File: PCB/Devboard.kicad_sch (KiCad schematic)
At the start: 0 parts

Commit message: Fix Section 1
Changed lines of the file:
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@@
 	(generator "eeschema")
 	(generator_version "10.0")
-	(paper "E")
-	(sheet
-		(at 292.735 15.24)
+	(paper "A1")
+	(sheet
+		(at 328.93 219.71)
 		(size 43.18 27.305)
 		(exclude_from_sim no)
@@
 		)
 		(property "Sheetname" "DDR4 Memory"
-			(at 292.735 14.5284 0)
+			(at 328.93 218.9984 0)
 			(show_name no)
 			(do_not_autoplace no)
@@
 		)
 		(property "Sheetfile" "schematics/04_Zynq/04b_Zynq_DDR4.kicad_sch"
-			(at 292.735 43.1296 0)
+			(at 328.93 247.5996 0)
 			(show_name no)
 			(do_not_autoplace no)
@@
 	)
 	(sheet
-		(at 158.115 15.24)
+		(at 194.31 219.71)
 		(size 45.085 27.305)
 		(exclude_from_sim no)
@@
 		)
 		(property "Sheetname" "Power Tree"
-			(at 158.115 14.5284 0)
+			(at 194.31 218.9984 0)
 			(show_name no)
 			(do_not_autoplace no)
@@
 		)
 		(property "Sheetfile" "schematics/03_Power_Tree/03_Power_Tree.kicad_sch"
-			(at 158.115 43.1296 0)
+			(at 194.31 247.5996 0)
 			(show_name no)
 			(do_not_autoplace no)
@@
 	)
 	(sheet
-		(at 88.265 15.24)
-		(size 44.45 27.305)
+		(at 118.745 15.24)
+		(size 43.815 27.94)
 		(exclude_from_sim no)
 		(in_bom yes)
@@
 		)
 		(property "Sheetname" "Battery.Charger,Fuel Gauge"
-			(at 88.265 14.5284 0)
+			(at 118.745 14.5284 0)
 			(show_name no)
 			(do_not_autoplace no)
@@
 		)
 		(property "Sheetfile" "schematics/02_Battery/Battery_Charger_FuelGauge.kicad_sch"
-			(at 88.265 43.1296 0)
+			(at 118.745 43.7646 0)
 			(show_name no)
 			(do_not_autoplace no)
@@
 	)
 	(sheet
-		(at 227.33 15.24)
+		(at 263.525 219.71)
 		(size 45.72 27.305)
 		(exclude_from_sim no)
@@
 		)
 		(property "Sheetname" "ZYNQ CORE"
-			(at 227.33 14.5284 0)
+			(at 263.525 218.9984 0)
 			(show_name no)
 			(do_not_autoplace no)
@@
 		)
 		(property "Sheetfile" "schematics/04_Zynq/04a_Zynq_Core.kicad_sch"
-			(at 227.33 43.1296 0)
+			(at 263.525 247.5996 0)
 			(show_name no)
 			(do_not_autoplace no)
@@
 	(sheet
 		(at 15.24 15.24)
-		(size 44.45 27.305)
+		(size 86.36 78.105)
 		(exclude_from_sim no)
 		(in_bom yes)
@@
 		)
 		(property "Sheetname" "Power,Input,Protection"
-			(at 15.24 14.5284 0)
+			(at 43.942 59.182 0)
 			(show_name no)
 			(do_not_autoplace no)
@@
 		)
 		(property "Sheetfile" "schematics/01_Power/Power_Input_Protection.kicad_sch"
-			(at 15.24 43.942 0)
-			(show_name no)
-			(do_not_autoplace no)
+			(at 27.178 60.198 0)
+			(show_name no)
+			(do_not_autoplace no)

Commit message: Zynq Added
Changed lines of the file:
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@@
 	)
 	(sheet
-		(at 194.31 219.71)
+		(at 243.205 45.72)
 		(size 45.085 27.305)
 		(exclude_from_sim no)
@@
 		)
 		(property "Sheetname" "Power Tree"
-			(at 194.31 218.9984 0)
+			(at 243.205 45.0084 0)
 			(show_name no)
 			(do_not_autoplace no)
@@
 		)
 		(property "Sheetfile" "schematics/03_Power_Tree/03_Power_Tree.kicad_sch"
-			(at 194.31 247.5996 0)
+			(at 243.205 73.6096 0)
 			(show_name no)
 			(do_not_autoplace no)
@@
 	(sheet
 		(at 118.745 15.24)
-		(size 43.815 27.94)
+		(size 88.9 78.105)
 		(exclude_from_sim no)
 		(in_bom yes)
 		(on_board yes)
 		(dnp no)
-		(fields_autoplaced yes)
 		(stroke
 			(width 0.1524)
@@
 		)
 		(property "Sheetname" "Battery.Charger,Fuel Gauge"
-			(at 118.745 14.5284 0)
+			(at 149.86 59.182 0)
 			(show_name no)
 			(do_not_autoplace no)
@@
 		)
 		(property "Sheetfile" "schematics/02_Battery/Battery_Charger_FuelGauge.kicad_sch"
-			(at 118.745 43.7646 0)
+			(at 132.334 93.98 0)
 			(show_name no)
 			(do_not_autoplace no)
@@
 		)
 		(property "Sheetfile" "schematics/01_Power/Power_Input_Protection.kicad_sch"
-			(at 27.178 60.198 0)
+			(at 29.464 94.234 0)
 			(show_name no)
 			(do_not_autoplace no)

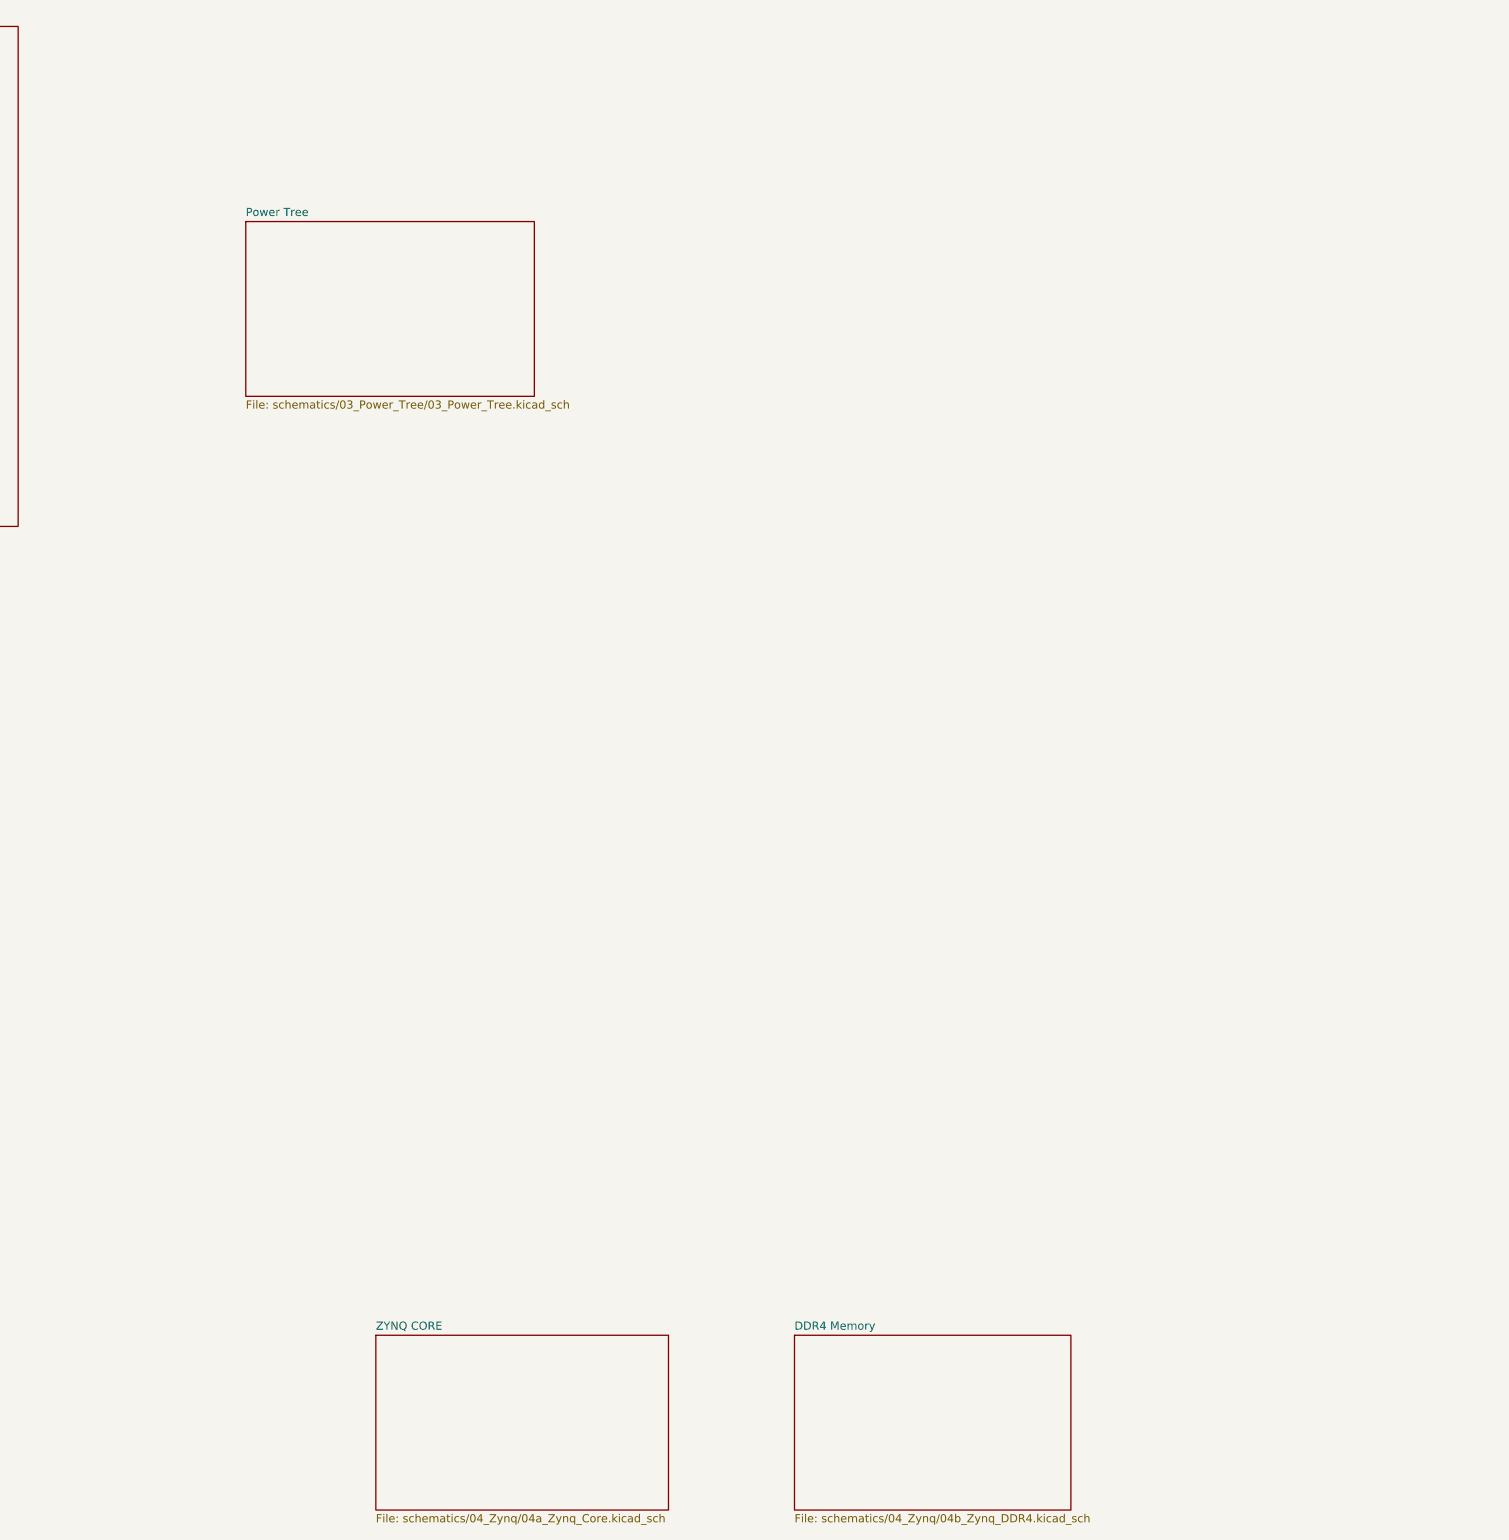
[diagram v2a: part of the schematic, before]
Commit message: Feat: Added zynq decoupling caps
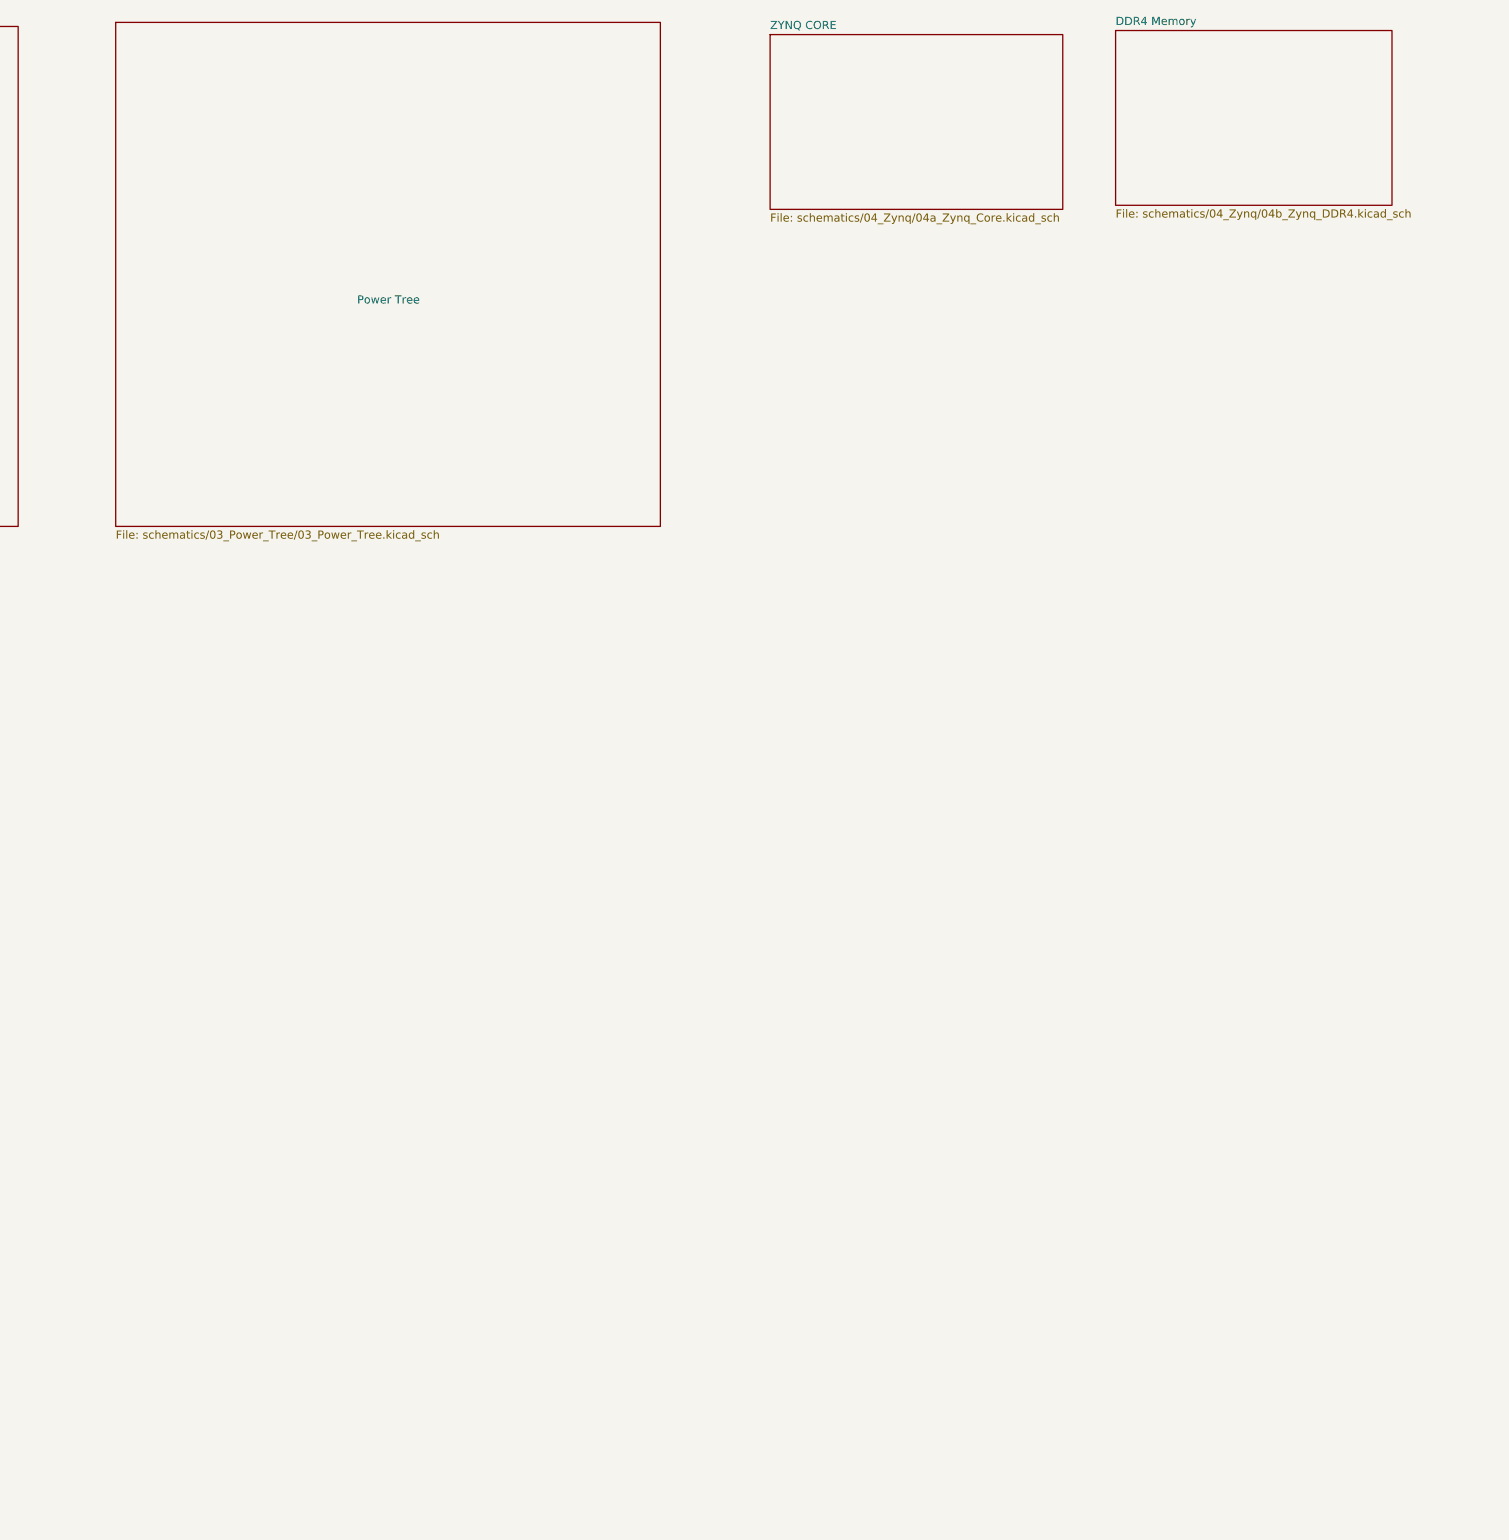
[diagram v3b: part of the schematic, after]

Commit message: Feat: Completed Zynq Core
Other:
- removed sheet DDR4 Memory
- removed sheet ZYNQ CORE
- added sheet Zynq Section (schematics\04_Zynq\04_Zynq.kicad_sch)
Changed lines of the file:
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@@
 	(paper "A2")
-	(sheet
-		(at 379.095 15.875)
-		(size 43.18 27.305)
-		(exclude_from_sim no)
-		(in_bom yes)
-		(on_board yes)
-		(dnp no)
-		(fields_autoplaced yes)
-		(stroke
-			(width 0.1524)
-			(type solid)
-		)
-		(fill
-			(color 0 0 0 0)
-		)
-		(property "Sheetname" "DDR4 Memory"
-			(at 379.095 15.1634 0)
-			(show_name no)
-			(do_not_autoplace no)
-			(effects
-				(font
-					(size 1.27 1.27)
-				)
-				(justify left bottom)
-			)
-		)
-		(property "Sheetfile" "schematics/04_Zynq/04b_Zynq_DDR4.kicad_sch"
-			(at 379.095 43.7646 0)
-			(show_name no)
-			(do_not_autoplace no)
-			(effects
-				(font
-					(size 1.27 1.27)
-				)
-				(justify left top)
-			)
-		)
-		(instances
-			(project "Devboard"
-				(path "/f4f7837f-dd80-4f77-b150-4534de1c10d6"
-					(page "6")
-				)
-			)
-		)
-	)
 	(sheet
 		(at 222.885 14.605)
@@
 	)
 	(sheet
-		(at 325.12 16.51)
-		(size 45.72 27.305)
-		(exclude_from_sim no)
-		(in_bom yes)
-		(on_board yes)
-		(dnp no)
-		(fields_autoplaced yes)
-		(stroke
-			(width 0.1524)
-			(type solid)
-		)
-		(fill
-			(color 0 0 0 0)
-		)
-		(property "Sheetname" "ZYNQ CORE"
-			(at 325.12 15.7984 0)
-			(show_name no)
-			(do_not_autoplace no)
-			(effects
-				(font
-					(size 1.27 1.27)
-				)
-				(justify left bottom)
-			)
-		)
-		(property "Sheetfile" "schematics/04_Zynq/04a_Zynq_Core.kicad_sch"
-			(at 325.12 44.3996 0)
-			(show_name no)
-			(do_not_autoplace no)
-			(effects
-				(font
-					(size 1.27 1.27)
-				)
-				(justify left top)
-			)
-		)
-		(instances
-			(project "Devboard"
-				(path "/f4f7837f-dd80-4f77-b150-4534de1c10d6"
-					(page "5")
-				)
-			)
-		)
-	)
-	(sheet
 		(at 15.24 15.24)
 		(size 86.36 78.105)
@@
 				)
 			)
+		)
+	)
+	(sheet
+		(at 323.215 14.605)
+		(size 82.55 78.74)
+		(exclude_from_sim no)
+		(in_bom yes)
+		(on_board yes)
+		(dnp no)
+		(fields_autoplaced yes)
+		(stroke
+			(width 0.1524)
+			(type solid)
+		)
+		(fill
+			(color 0 0 0 0)
+		)
+		(property "Sheetname" "Zynq Section"
+			(at 323.215 13.8934 0)
+			(show_name no)
+			(do_not_autoplace no)
+			(effects
+				(font
+					(size 1.27 1.27)
+				)
+				(justify left bottom)
+			)
+		)
+		(property "Sheetfile" "schematics\\04_Zynq\\04_Zynq.kicad_sch"
+			(at 323.215 93.9296 0)
+			(show_name no)
+			(do_not_autoplace no)
+			(effects
+				(font
+					(size 1.27 1.27)
+				)
+				(justify left top)
+			)
+		)
+		(instances
+			(project "Devboard"
+				(path "/f4f7837f-dd80-4f77-b150-4534de1c10d6"
+					(page "5")
+				)
+			)

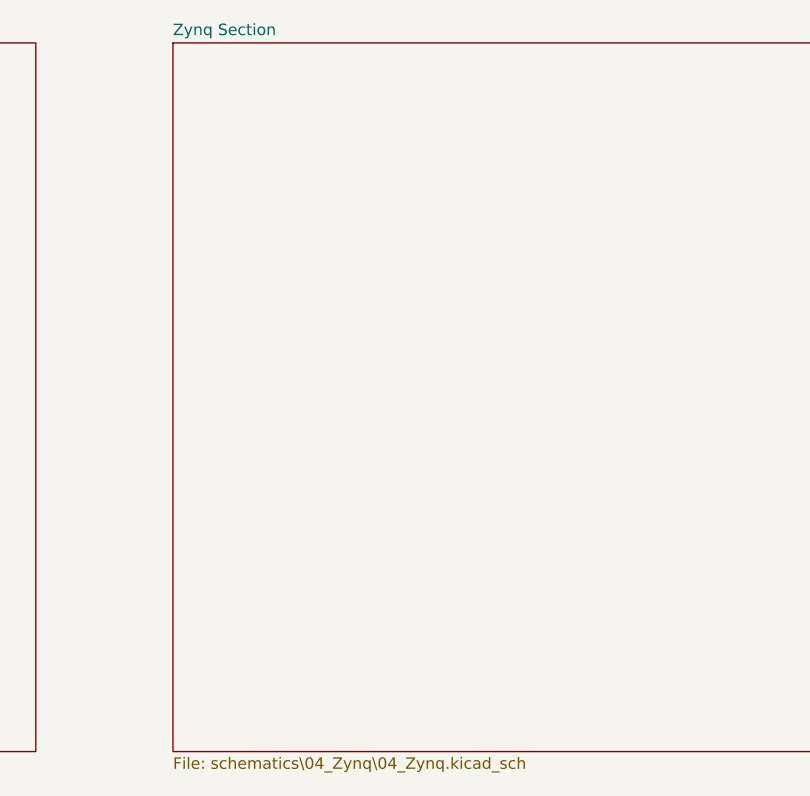
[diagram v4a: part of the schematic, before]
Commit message: Feat: DDR4 Memory added
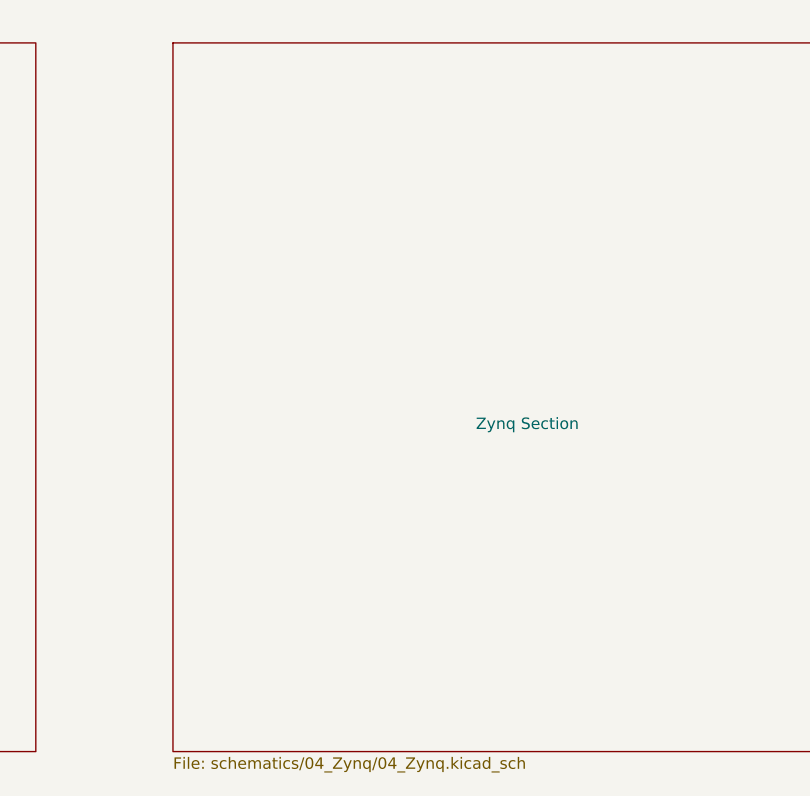
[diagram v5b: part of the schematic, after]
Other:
- sheet Zynq Section: file schematics\04_Zynq\04_Zynq.kicad_sch -> schematics/04_Zynq/04_Zynq.kicad_sch
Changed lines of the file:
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@@
 		(on_board yes)
 		(dnp no)
-		(fields_autoplaced yes)
 		(stroke
 			(width 0.1524)
@@
 		)
 		(property "Sheetname" "Zynq Section"
-			(at 323.215 13.8934 0)
+			(at 356.87 57.658 0)
 			(show_name no)
 			(do_not_autoplace no)
@@
 			)
 		)
-		(property "Sheetfile" "schematics\\04_Zynq\\04_Zynq.kicad_sch"
+		(property "Sheetfile" "schematics/04_Zynq/04_Zynq.kicad_sch"
 			(at 323.215 93.9296 0)
 			(show_name no)

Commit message: feat: Section 4 Done
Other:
- added sheet Zynq Section1 (schematics/04_Zynq/04_Zynq.kicad_sch)
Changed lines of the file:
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@@
+	)
+	(sheet
+		(at 419.735 14.605)
+		(size 82.55 78.74)
+		(exclude_from_sim no)
+		(in_bom yes)
+		(on_board yes)
+		(dnp no)
+		(stroke
+			(width 0.1524)
+			(type solid)
+		)
+		(fill
+			(color 0 0 0 0)
+		)
+		(property "Sheetname" "Zynq Section1"
+			(at 453.39 57.658 0)
+			(show_name no)
+			(do_not_autoplace no)
+			(effects
+				(font
+					(size 1.27 1.27)
+				)
+				(justify left bottom)
+			)
+		)
+		(property "Sheetfile" "schematics/04_Zynq/04_Zynq.kicad_sch"
+			(at 419.735 93.9296 0)
+			(show_name no)
+			(do_not_autoplace no)
+			(effects
+				(font
+					(size 1.27 1.27)
+				)
+				(justify left top)
+			)
+		)
+		(instances
+			(project "Devboard"
+				(path "/f4f7837f-dd80-4f77-b150-4534de1c10d6"
+					(page "10")
+				)
+			)
+		)
 	)
 	(sheet

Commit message: Feat : Schematics Complete
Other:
- sheet Zynq Section1 renamed Clocking
- added sheet Analog | RF (schematics/07_Analog_RF/07_Analog_RF.kicad_sch)
- added sheet Expansion (schematics\12_Expansion\12_Expansion.kicad_sch)
- added sheet Harvester, BMC, Telemetry (schematics\10_Harvester_BMC_Telemetry\10_Harvester_BMC_Telemetry.kicad_sch)
- added sheet RTC & Security (schematics\09_RTC_Security\09_RTC_Security.kicad_sch)
- added sheet Sensors and GNSS (schematics\08_Sensors_GNSS\08_Sensors_GNSS.kicad_sch)
- added sheet Video (schematics/06_Video/06_Video.kicad_sch)
- added sheet ePaper Ink Display (schematics\11_ePaper\11_ePaper.kicad_sch)
- sheet Clocking: file schematics/04_Zynq/04_Zynq.kicad_sch -> schematics/05_Clocking/05_Clocking.kicad_sch
- note added: "Fusion Board : Master Page"
